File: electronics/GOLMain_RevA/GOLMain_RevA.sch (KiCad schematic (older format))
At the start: 31 parts, among them P1 CONN_LEDS, P2 CONN_SERIAL, P3 CONN_READERS, P4 CONN_POWER, Q1 BSS138, Q2 BSS138, SW1 SW_PUSH, SW2 SW_PUSH, U1 LM1117-3.3, U2 ESP8266-12E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

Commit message: updated schematic and layout for proposed RevA
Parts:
- U4: renamed from U?; footprint SO-8 -> Power_Integrations:SO-8
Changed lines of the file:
@@
 V33
 $Comp
-L +3.3V #PWR01
+L +3.3V #PWR3
 U 1 1 58B19A2F
 P 3550 1750
-F 0 "#PWR01" H 3550 1600 50  0001 C CNN
+F 0 "#PWR3" H 3550 1600 50  0001 C CNN
 F 1 "+3.3V" H 3550 1890 50  0000 C CNN
 F 2 "" H 3550 1750 50  0000 C CNN
@@
 $EndComp
 $Comp
-L GND #PWR02
+L GND #PWR2
 U 1 1 58B19D95
 P 3000 2475
-F 0 "#PWR02" H 3000 2225 50  0001 C CNN
+F 0 "#PWR2" H 3000 2225 50  0001 C CNN
 F 1 "GND" H 3000 2325 50  0000 C CNN
 F 2 "" H 3000 2475 50  0000 C CNN
@@
 $EndComp
 $Comp
-L +12V #PWR03
+L +12V #PWR1
 U 1 1 58B19DE8
 P 2775 1825
-F 0 "#PWR03" H 2775 1675 50  0001 C CNN
+F 0 "#PWR1" H 2775 1675 50  0001 C CNN
 F 1 "+12V" H 2775 1965 50  0000 C CNN
 F 2 "" H 2775 1825 50  0000 C CNN
@@
 Connection ~ 3000 2350
 $Comp
-L VCC #PWR04
+L VCC #PWR4
 U 1 1 58B1A133
 P 3750 1750
-F 0 "#PWR04" H 3750 1600 50  0001 C CNN
+F 0 "#PWR4" H 3750 1600 50  0001 C CNN
 F 1 "VCC" H 3750 1900 50  0000 C CNN
 F 2 "" H 3750 1750 50  0000 C CNN
@@
 Connection ~ 2775 2350
 $Comp
-L SP3485CN U?
+L SP3485CN U4
 U 1 1 58B21144
 P 7575 3250
-F 0 "U?" H 7275 3600 50  0000 L CNN
+F 0 "U4" H 7275 3600 50  0000 L CNN
 F 1 "SP3485CN" H 7675 3600 50  0000 L CNN
-F 2 "SO-8" H 7575 3250 50  0000 C CIN
+F 2 "Power_Integrations:SO-8" H 7575 3250 50  0000 C CIN
 F 3 "" H 7575 3250 50  0000 C CNN
 	1    7575 3250

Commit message: updated main board schematic and layout
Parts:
- removed P1: CONN_LEDS, Pin_Headers:Pin_Header_Angled_1x02, symbol CONN_01X02
- removed P2: CONN_SERIAL, Pin_Headers:Pin_Header_Angled_1x02, symbol CONN_01X02
- removed P4: CONN_POWER, Pin_Headers:Pin_Header_Angled_1x02, symbol CONN_01X02
- removed SW1, SW2: SW_PUSH, Buttons_Switches_ThroughHole:SW_PUSH_SMALL, symbol SW_PUSH
- added C4: 100uF 50V, Capacitors_ThroughHole:C_Radial_D8_L13_P3.8, symbol CP1
- added P1: CONN_ID_0, Pin_Headers:Pin_Header_Straight_1x03, symbol CONN_01X03
- added P10: CONN_ID_6, Pin_Headers:Pin_Header_Straight_1x03, symbol CONN_01X03
- added P11: CONN_ID_7, Pin_Headers:Pin_Header_Straight_1x03, symbol CONN_01X03
- added P12: CONN_LED, Pin_Headers:Pin_Header_Angled_1x04, symbol CONN_01X04
- added P2: CONN_ID_1, Pin_Headers:Pin_Header_Straight_1x03, symbol CONN_01X03
- added P4: CONN_ID_2, Pin_Headers:Pin_Header_Straight_1x03, symbol CONN_01X03
- added P5: CONN_MAIN1, Connect:AK300-4, symbol CONN_01X04
- added P6: CONN_MAIN2, Connect:AK300-4, symbol CONN_01X04
- added P7: CONN_ID_3, Pin_Headers:Pin_Header_Straight_1x03, symbol CONN_01X03
- added P8: CONN_ID_4, Pin_Headers:Pin_Header_Straight_1x03, symbol CONN_01X03
- added P9: CONN_ID_5, Pin_Headers:Pin_Header_Straight_1x03, symbol CONN_01X03
- added Q3, Q4, Q5: BSS138, TO_SOT_Packages_SMD:SOT-23, symbol BSS138
- added R17, R18, R19, R20, R21, R22, R23, R24: 10K, Resistors_SMD:R_1206, symbol R
- added SW1, SW2: SW_PROG, Buttons_Switches_ThroughHole:SW_PUSH_SMALL, symbol SW_PUSH_SMALL_H
- added U5: MAX485Module, Housings_DIP:DIP-8_W7.62mm_LongPads, symbol MAX485Module
- C3: value 1F -> 100uF 50V
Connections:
- net labels added: A, B, EN_MAX, EN_MAX33, EN_MAX50, GPIO0, GPIO0_OUT, GPIO15, GPIO15_OUT, GPIO2, GPIO2_OUT, RESET, RX33, RX50, TX33, TX50, V50
- net labels removed: RX, TX
- wire segments 29 -> 67
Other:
- note added: "2-6V Supply for SN74HC165D"
- note added: "ESP8266\nGPIO15 pull down\nGPIO0 pull up, switch to gnd\nGPIO2 pull up\n0,2,15 Only as Outputs\nCan't use SPI"
- note added: "MAX485 Module is 5V\nHIGH is 3.5V\nCan't use GPIO15\n due to MOSFET pull up"
- note added: "SP3485 is 3.3V\nLOW is Receive\nGPIO15 is already default LOW"
- moved on the sheet: C1, C2, C3, P3, Q1, Q2, R1, R10, R11, R12, R13, R14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

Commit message: updated schematics and part selection for layout
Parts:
- removed P3: CONN_READERS, Pin_Headers:Pin_Header_Angled_1x04, symbol CONN_01X04
- removed R1, R2, R3, R4, R5, R6, R7, R8: 10K, Resistors_SMD:R_1206, symbol R
- added C5, C6: 0.1uF, Capacitors_SMD:C_0805, symbol C
- added P13: CONN_FTDI, Pin_Headers:Pin_Header_Angled_1x06, symbol CONN_01X06
- added P14: CONN_V50SEL, Pin_Headers:Pin_Header_Straight_1x02, symbol CONN_01X02
- added P3: CONN_READERS, Pin_Headers:Pin_Header_Straight_2x03, symbol CONN_02X03
- added R25: 56, Resistors_SMD:R_1206, symbol R
- added R26: 39, Resistors_SMD:R_1206, symbol R
- added RP1, RP2: R_PACK4_10K, Resistors_SMD:R_Array_Convex_4x1206, symbol R_PACK4
- added U6: LM78L05ACZ, TO_SOT_Packages_THT:TO-92_Rugged, symbol LM78L05ACZ
- P12: footprint Pin_Headers:Pin_Header_Angled_1x04 -> Connect:AK300-4
- R13, R14, R15, R16: value 10K -> 1K
- SW1: value SW_PROG -> SW_RESET
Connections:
- net labels added: CTS, RTS, V50D
- net labels removed: EN_MAX33
- wire segments 67 -> 76
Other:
- note added: "ESP8266 GPIO\nMax Current is 12mA\n3.3/12mA = 275 Ohm\n1K Ohm OK"
- note added: "SP3485 is 3.3V\nLOW is Receive\nGPIO15 is already default LOW\nBut need to pull high\nfor 5V Level Shifting"
- note added: "Voltage Divider\nFor 5V supply\nif needed"
- note removed: "SP3485 is 3.3V\nLOW is Receive\nGPIO15 is already default LOW"
- moved on the sheet: C1, C2, C3, C4, P5, P6, U1

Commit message: near final version of pcb layout
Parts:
- removed P3: CONN_READERS, Pin_Headers:Pin_Header_Straight_2x03, symbol CONN_02X03
- added C7: 0.1uF, Capacitors_SMD:C_0805, symbol C
- added P15: CONN_AB_RES, Pin_Headers:Pin_Header_Straight_1x02, symbol CONN_01X02
- added P16: CONN_V12V50, Pin_Headers:Pin_Header_Straight_1x02, symbol CONN_01X02
- added P17: CONN_LEDCLK, Pin_Headers:Pin_Header_Straight_1x02, symbol CONN_01X02
- added P18: CONN_LEDDATA, Pin_Headers:Pin_Header_Straight_1x02, symbol CONN_01X02
- added P19: CONN_TX3350, Pin_Headers:Pin_Header_Straight_1x02, symbol CONN_01X02
- added P20: CONN_EN3350, Pin_Headers:Pin_Header_Straight_1x02, symbol CONN_01X02
- added P21: CONN_RX3350, Pin_Headers:Pin_Header_Straight_1x02, symbol CONN_01X02
- added P3: CONN_READERS, Sockets_MOLEX_KK-System:Socket_MOLEX-KK-RM2-54mm_Lock_4pin_straight, symbol CONN_01X04
- added R1, R2: 470, Resistors_SMD:R_1206, symbol R
- added R3: 100, Resistors_SMD:R_1206, symbol R
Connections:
- wire segments 76 -> 78
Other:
- note added: "Bridge 12V to 5V\nIf Input Voltage\nis actually 5V"
- note added: "Default\nDirectly Connected"
- note added: "END Node should\nuse a resistor to\ndecrease reflections"
- moved on the sheet: P12, Q2, Q4, Q5, R14, R16, R18, R20, R23, R24, U5

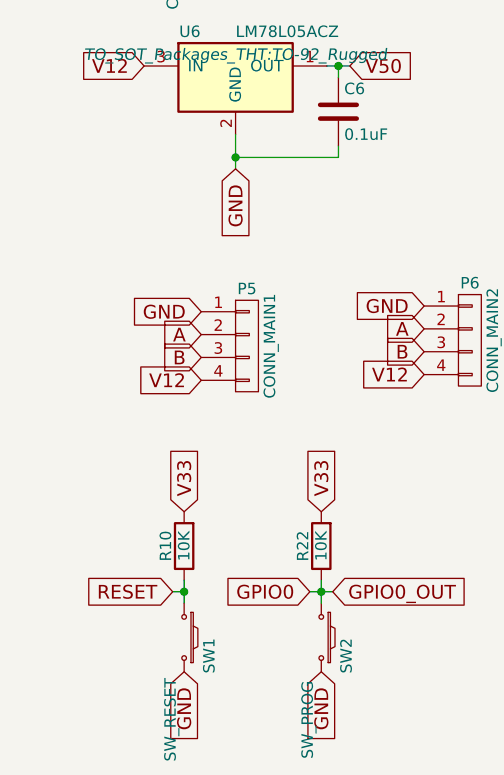
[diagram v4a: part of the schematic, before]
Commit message: added basic station string test firmware
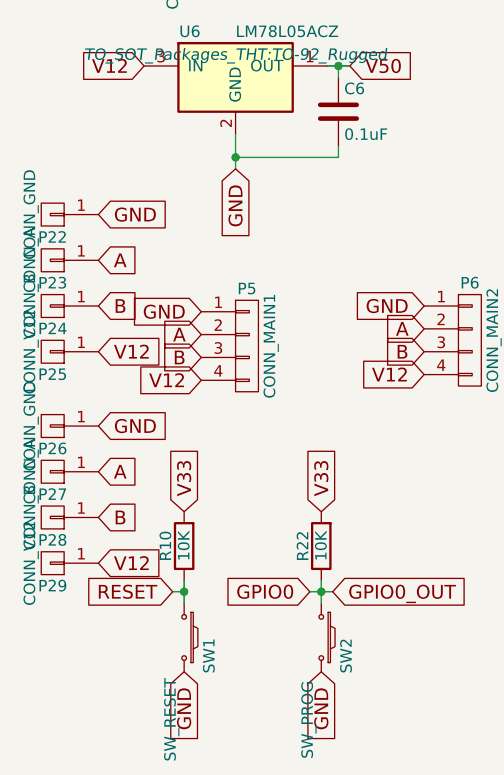
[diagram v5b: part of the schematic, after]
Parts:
- added P22, P26: CONN_GND, Wire_Pads:SolderWirePad_single_1-5mmDrill, symbol CONN_01X01
- added P23, P27: CONN_A, Wire_Pads:SolderWirePad_single_0-8mmDrill, symbol CONN_01X01
- added P24, P28: CONN_B, Wire_Pads:SolderWirePad_single_0-8mmDrill, symbol CONN_01X01
- added P25, P29: CONN_V12, Wire_Pads:SolderWirePad_single_1-5mmDrill, symbol CONN_01X01
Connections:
- net +12V: now also P25.1 (P1), P29.1 (P1)
- net A: now also P23.1 (P1), P27.1 (P1)
- net B: now also P24.1 (P1), P28.1 (P1)
- net GND: now also P22.1 (P1), P26.1 (P1)
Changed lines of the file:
@@
 Sheet 1 1
 Title "GOLMain"
-Date "2017-03-17"
+Date "2017-03-23"
 Rev "A"
 Comp "Matthew Swarts"
@@
 Text Notes 8475 2050 0    60   ~ 0
 Default\nDirectly Connected
+$Comp
+L CONN_01X01 P22
+U 1 1 58D373E5
+P 675 2925
+F 0 "P22" H 675 3025 50  0000 C CNN
+F 1 "CONN_GND" V 775 2925 50  0000 C CNN
+F 2 "Wire_Pads:SolderWirePad_single_1-5mmDrill" H 675 2925 50  0001 C CNN
+F 3 "" H 675 2925 50  0000 C CNN
+	1    675  2925
+	-1   0    0    1
+$EndComp
+$Comp
+L CONN_01X01 P23
+U 1 1 58D37FCA
+P 675 3125
+F 0 "P23" H 675 3225 50  0000 C CNN
+F 1 "CONN_A" V 775 3125 50  0000 C CNN
+F 2 "Wire_Pads:SolderWirePad_single_0-8mmDrill" H 675 3125 50  0001 C CNN
+F 3 "" H 675 3125 50  0000 C CNN
+	1    675  3125
+	-1   0    0    1
+$EndComp
+$Comp
+L CONN_01X01 P24
+U 1 1 58D380CA
+P 675 3325
+F 0 "P24" H 675 3425 50  0000 C CNN
+F 1 "CONN_B" V 775 3325 50  0000 C CNN
+F 2 "Wire_Pads:SolderWirePad_single_0-8mmDrill" H 675 3325 50  0001 C CNN
+F 3 "" H 675 3325 50  0000 C CNN
+	1    675  3325
+	-1   0    0    1
+$EndComp
+$Comp
+L CONN_01X01 P25
+U 1 1 58D381B5
+P 675 3525
+F 0 "P25" H 675 3625 50  0000 C CNN
+F 1 "CONN_V12" V 775 3525 50  0000 C CNN
+F 2 "Wire_Pads:SolderWirePad_single_1-5mmDrill" H 675 3525 50  0001 C CNN
+F 3 "" H 675 3525 50  0000 C CNN
+	1    675  3525
+	-1   0    0    1
+$EndComp
+$Comp
+L CONN_01X01 P26
+U 1 1 58D386A7
+P 675 3850
+F 0 "P26" H 675 3950 50  0000 C CNN
+F 1 "CONN_GND" V 775 3850 50  0000 C CNN
+F 2 "Wire_Pads:SolderWirePad_single_1-5mmDrill" H 675 3850 50  0001 C CNN
+F 3 "" H 675 3850 50  0000 C CNN
+	1    675  3850
+	-1   0    0    1
+$EndComp
+$Comp
+L CONN_01X01 P27
+U 1 1 58D386AD
+P 675 4050
+F 0 "P27" H 675 4150 50  0000 C CNN
+F 1 "CONN_A" V 775 4050 50  0000 C CNN
+F 2 "Wire_Pads:SolderWirePad_single_0-8mmDrill" H 675 4050 50  0001 C CNN
+F 3 "" H 675 4050 50  0000 C CNN
+	1    675  4050
+	-1   0    0    1
+$EndComp
+$Comp
+L CONN_01X01 P28
+U 1 1 58D386B3
+P 675 4250
+F 0 "P28" H 675 4350 50  0000 C CNN
+F 1 "CONN_B" V 775 4250 50  0000 C CNN
+F 2 "Wire_Pads:SolderWirePad_single_0-8mmDrill" H 675 4250 50  0001 C CNN
+F 3 "" H 675 4250 50  0000 C CNN
+	1    675  4250
+	-1   0    0    1
+$EndComp
+$Comp
+L CONN_01X01 P29
+U 1 1 58D386B9
+P 675 4450
+F 0 "P29" H 675 4550 50  0000 C CNN
+F 1 "CONN_V12" V 775 4450 50  0000 C CNN
+F 2 "Wire_Pads:SolderWirePad_single_1-5mmDrill" H 675 4450 50  0001 C CNN
+F 3 "" H 675 4450 50  0000 C CNN
+	1    675  4450
+	-1   0    0    1
+$EndComp
+Text GLabel 875  2925 2    60   Input ~ 0
+GND
+Text GLabel 875  3125 2    60   Input ~ 0
+A
+Text GLabel 875  3325 2    60   Input ~ 0
+B
+Text GLabel 875  3525 2    60   Input ~ 0
+V12
+Text GLabel 875  3850 2    60   Input ~ 0
+GND
+Text GLabel 875  4050 2    60   Input ~ 0
+A
+Text GLabel 875  4250 2    60   Input ~ 0
+B
+Text GLabel 875  4450 2    60   Input ~ 0
+V12
 $EndSCHEMATC

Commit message: version 1015; change MPR121 setup while loop to a single begin call
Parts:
- Q1, Q2, Q3, Q4, Q5: symbol BSS138 -> BSS138-RESCUE-GOLMain_RevA
- U1: symbol LM1117-3.3 -> LM1117-3.3-RESCUE-GOLMain_RevA
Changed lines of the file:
@@
 EESchema Schematic File Version 2
+LIBS:GOLMain_RevA-rescue
 LIBS:power
 LIBS:device
@@
 $EndComp
 $Comp
-L LM1117-3.3 U1
+L LM1117-3.3-RESCUE-GOLMain_RevA U1
 U 1 1 58B0E4BE
 P 2700 1125
@@
 GND
 $Comp
-L BSS138 Q1
+L BSS138-RESCUE-GOLMain_RevA Q1
 U 1 1 58B1C347
 P 7650 2375
@@
 V50
 $Comp
-L BSS138 Q2
+L BSS138-RESCUE-GOLMain_RevA Q2
 U 1 1 58B1DEC3
 P 7650 3375
@@
 V33
 $Comp
-L BSS138 Q3
+L BSS138-RESCUE-GOLMain_RevA Q3
 U 1 1 58C34185
 P 10350 2850
@@
 TX50
 $Comp
-L BSS138 Q4
+L BSS138-RESCUE-GOLMain_RevA Q4
 U 1 1 58C3545B
 P 10350 4150
@@
 MAX485 Module is 5V\nHIGH is 3.5V\nCan't use GPIO15\n  due to MOSFET pull up
 $Comp
-L BSS138 Q5
+L BSS138-RESCUE-GOLMain_RevA Q5
 U 1 1 58C5DEBC
 P 10350 5475
